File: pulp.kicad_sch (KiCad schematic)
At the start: 0 parts

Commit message: finalized a lot of sub-modules
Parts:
- added C5, C7: 4.7uF, Capacitor_SMD:C_0201_0603Metric, symbol Device:C
- added C6, C8: 1uF, Capacitor_SMD:C_0201_0603Metric, symbol Device:C
- added D1, D2: ESD9B5.0ST5G, Diode_SMD:D_SOD-923, symbol Diode:ESD9B5.0ST5G
- added D3: LED_ARGB, symbol Device:LED_ARGB
- added J2, J3: Conn_01x02_Pin, Connector_PinHeader_2.54mm:PinHeader_1x02_P2.54mm_Horizontal, symbol Connector:Conn_01x02_Pin
- added J4, J5: Conn_01x03_Pin, Connector_PinHeader_2.54mm:PinHeader_1x03_P2.54mm_Horizontal, symbol Connector:Conn_01x03_Pin
- added J6: Conn_01x09_Pin, symbol Connector:Conn_01x09_Pin
- added J7: USB_C_Receptacle, Connector_USB:USB_C_Receptacle_CNCTech_C-ARA1-AK51X, symbol Connector:USB_C_Receptacle
- added Q1, Q2, Q3: BSS138, Package_TO_SOT_SMD:SOT-23, symbol Transistor_FET:BSS138
- added R19, R20, R9: 510, symbol Device:R
- added R21, R22, R23: 27, symbol Device:R
- added R4, R5: 5.1K, symbol Device:R
- added R6: 10K, Resistor_SMD:R_0201_0603Metric, symbol Device:R
- added R7, R8: 1K, symbol Device:R
- added SW1, SW2: SW_Push, symbol Switch:SW_Push
- added U4: AP7361C-33E, Package_TO_SOT_SMD:SOT-223-3_TabPin2, symbol Regulator_Linear:AP7361C-33E
- added U5: W25Q128JVS, Package_SO:SOIC-8_5.23x5.23mm_P1.27mm, symbol Memory_Flash:W25Q128JVS
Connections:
- new net: Q2.3 (D), R19.1
- new net: D3.3 (GK), R19.2
- new net: J7.B5 (CC2), R4.1
- new net: Q3.3 (D), R9.1
- new net: D3.4 (BK), R9.2
- new net: Q1.1 (G), R21.2
- new net: Q1.3 (D), R20.1
- new net: D3.2 (RK), R20.2
- new net: Q2.1 (G), R22.2
- new net: J7.A5 (CC1), R5.1
- new net: Q3.1 (G), R23.2
- new net: R7.1, SW2.2
- new net: R8.1, SW1.2
- new net +5V: C5.1, C6.1, D3.1 (A), J6.2 (Pin_2), J7.A4 (VBUS), J7.A9 (VBUS), J7.B4 (VBUS), J7.B9 (VBUS), U4.1 (VI)
- new net 3V3: C7.1, C8.2, J6.3 (Pin_3), R6.2, U4.3 (VO), U5.8 (VCC)
- new net BATT_V: J4.3 (Pin_3), J5.3 (Pin_3)
- new net GND: C5.2, C6.2, C7.2, C8.1, D1.1 (A1), D2.1 (A1), J4.1 (Pin_1), J5.1 (Pin_1), J6.1 (Pin_1), J7.A1 (GND), J7.A12 (GND), J7.B1 (GND), J7.B12 (GND), Q1.2 (S), Q2.2 (S), Q3.2 (S), R4.2, R5.2, SW1.1, SW2.1, U4.2 (GND), U5.4 (GND)
- new net GP0: J6.4 (Pin_4)
- new net GP1: J6.5 (Pin_5)
- new net GP2: J6.6 (Pin_6)
- new net GP3: J6.7 (Pin_7)
- new net GP4: J6.8 (Pin_8)
- new net GP5: J6.9 (Pin_9)
- new net I2C_SCL 0: J3.2 (Pin_2)
- new net I2C_SCL 1: J2.2 (Pin_2)
- new net I2C_SDA 0: J3.1 (Pin_1)
- new net I2C_SDA 1: J2.1 (Pin_1)
- new net LED_B: R23.1
- new net LED_G: R22.1
- new net LED_R: R21.1
- new net PWM_LEFT: J5.2 (Pin_2)
- new net PWM_RIGHT: J4.2 (Pin_2)
- new net Q0: U5.5 (DI(IO0))
- new net Q1: U5.2 (DO(IO1))
- new net Q2: U5.3 (IO2)
- new net Q3: U5.7 (IO3)
- new net Q_SCLK: U5.6 (CLK)
- new net Q_SS: R6.1, R8.2, U5.1 (~{CS})
- new net USB_D+: D1.2 (A2), J7.A6 (D+), J7.B6 (D+)
- new net USB_D-: D2.2 (A2), J7.A7 (D-), J7.B7 (D-)
- new net ~{RST}: R7.2
- no-connect marks 0 -> 11
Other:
- sheet RP2040 ports: added LED_B (GPIO_17), LED_G (GPIO_16), LED_R (GPIO_15); removed SWCLK, SWD
- note added: "I2C 0"
- note added: "I2C 1"

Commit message: NO ERC ERRORS!!!!
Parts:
- D3: footprint (none) -> LED_SMD:LED_RGB_1210
- J6: footprint (none) -> Connector_PinHeader_2.54mm:PinHeader_1x09_P2.54mm_Vertical
- R19, R20, R21, R22, R23, R4, R5, R7, R8, R9: footprint (none) -> Resistor_SMD:R_0201_0603Metric
- SW1, SW2: footprint (none) -> Button_Switch_SMD:SW_Push_SPST_NO_Alps_SKRK
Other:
- sheet MAX_8C GNSS ports: added none; removed SCL, SDA
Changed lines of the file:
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@@
       (effects (font (size 1.27 1.27)))
     )
-    (property "Footprint" "" (at 257.048 39.37 90)
+    (property "Footprint" "Resistor_SMD:R_0201_0603Metric" (at 257.048 39.37 90)
       (effects (font (size 1.27 1.27)) hide)
     )
@@
       (effects (font (size 1.27 1.27)))
     )
-    (property "Footprint" "" (at 64.262 43.18 90)
+    (property "Footprint" "Resistor_SMD:R_0201_0603Metric" (at 64.262 43.18 90)
       (effects (font (size 1.27 1.27)) hide)
     )
@@
       (effects (font (size 1.27 1.27)))
     )
-    (property "Footprint" "" (at 262.128 39.37 90)
+    (property "Footprint" "Resistor_SMD:R_0201_0603Metric" (at 262.128 39.37 90)
       (effects (font (size 1.27 1.27)) hide)
     )
@@
       (effects (font (size 1.27 1.27)))
     )
-    (property "Footprint" "" (at 251.968 39.37 90)
+    (property "Footprint" "Resistor_SMD:R_0201_0603Metric" (at 251.968 39.37 90)
       (effects (font (size 1.27 1.27)) hide)
     )
@@
       (effects (font (size 1.27 1.27)))
     )
-    (property "Footprint" "" (at 69.342 43.18 90)
+    (property "Footprint" "Resistor_SMD:R_0201_0603Metric" (at 69.342 43.18 90)
       (effects (font (size 1.27 1.27)) hide)
     )
@@
       (effects (font (size 1.27 1.27)))
     )
-    (property "Footprint" "" (at 200.66 152.908 90)
+    (property "Footprint" "Resistor_SMD:R_0201_0603Metric" (at 200.66 152.908 90)
       (effects (font (size 1.27 1.27)) hide)
     )
@@
       (effects (font (size 1.27 1.27)))
     )
-    (property "Footprint" "" (at 240.03 53.848 90)
+    (property "Footprint" "Resistor_SMD:R_0201_0603Metric" (at 240.03 53.848 90)
       (effects (font (size 1.27 1.27)) hide)
     )
@@
       (effects (font (size 1.27 1.27)))
     )
-    (property "Footprint" "" (at 256.54 26.67 0)
+    (property "Footprint" "LED_SMD:LED_RGB_1210" (at 256.54 26.67 0)
       (effects (font (size 1.27 1.27)) hide)
     )
@@
       (effects (font (size 1.27 1.27)))
     )
-    (property "Footprint" "" (at 200.66 140.208 90)
+    (property "Footprint" "Resistor_SMD:R_0201_0603Metric" (at 200.66 140.208 90)
       (effects (font (size 1.27 1.27)) hide)
     )
@@
       (effects (font (size 1.27 1.27)))
     )
-    (property "Footprint" "" (at 187.96 133.35 0)
+    (property "Footprint" "Button_Switch_SMD:SW_Push_SPST_NO_Alps_SKRK" (at 187.96 133.35 0)
       (effects (font (size 1.27 1.27)) hide)
     )
@@
       (effects (font (size 1.27 1.27)))
     )
-    (property "Footprint" "" (at 240.03 64.008 90)
+    (property "Footprint" "Resistor_SMD:R_0201_0603Metric" (at 240.03 64.008 90)
       (effects (font (size 1.27 1.27)) hide)
     )
@@
       (effects (font (size 1.27 1.27)))
     )
-    (property "Footprint" "" (at 240.03 74.168 90)
+    (property "Footprint" "Resistor_SMD:R_0201_0603Metric" (at 240.03 74.168 90)
       (effects (font (size 1.27 1.27)) hide)
     )
@@
       (effects (font (size 1.27 1.27)))
     )
-    (property "Footprint" "" (at 187.96 146.05 0)
+    (property "Footprint" "Button_Switch_SMD:SW_Push_SPST_NO_Alps_SKRK" (at 187.96 146.05 0)
       (effects (font (size 1.27 1.27)) hide)
     )
@@
       (effects (font (size 1.27 1.27)) (justify right))
     )
-    (property "Footprint" "" (at 232.41 147.32 0)
+    (property "Footprint" "Connector_PinHeader_2.54mm:PinHeader_1x09_P2.54mm_Vertical" (at 232.41 147.32 0)
       (effects (font (size 1.27 1.27)) hide)
     )
@@
       (effects (font (size 1.27 1.27)) (justify left))
     )
-    (pin "SDA" input (at 177.8 90.17 180)
-      (effects (font (size 1.27 1.27)) (justify left))
-    )
-    (pin "SCL" input (at 177.8 87.63 180)
-      (effects (font (size 1.27 1.27)) (justify left))
-    )

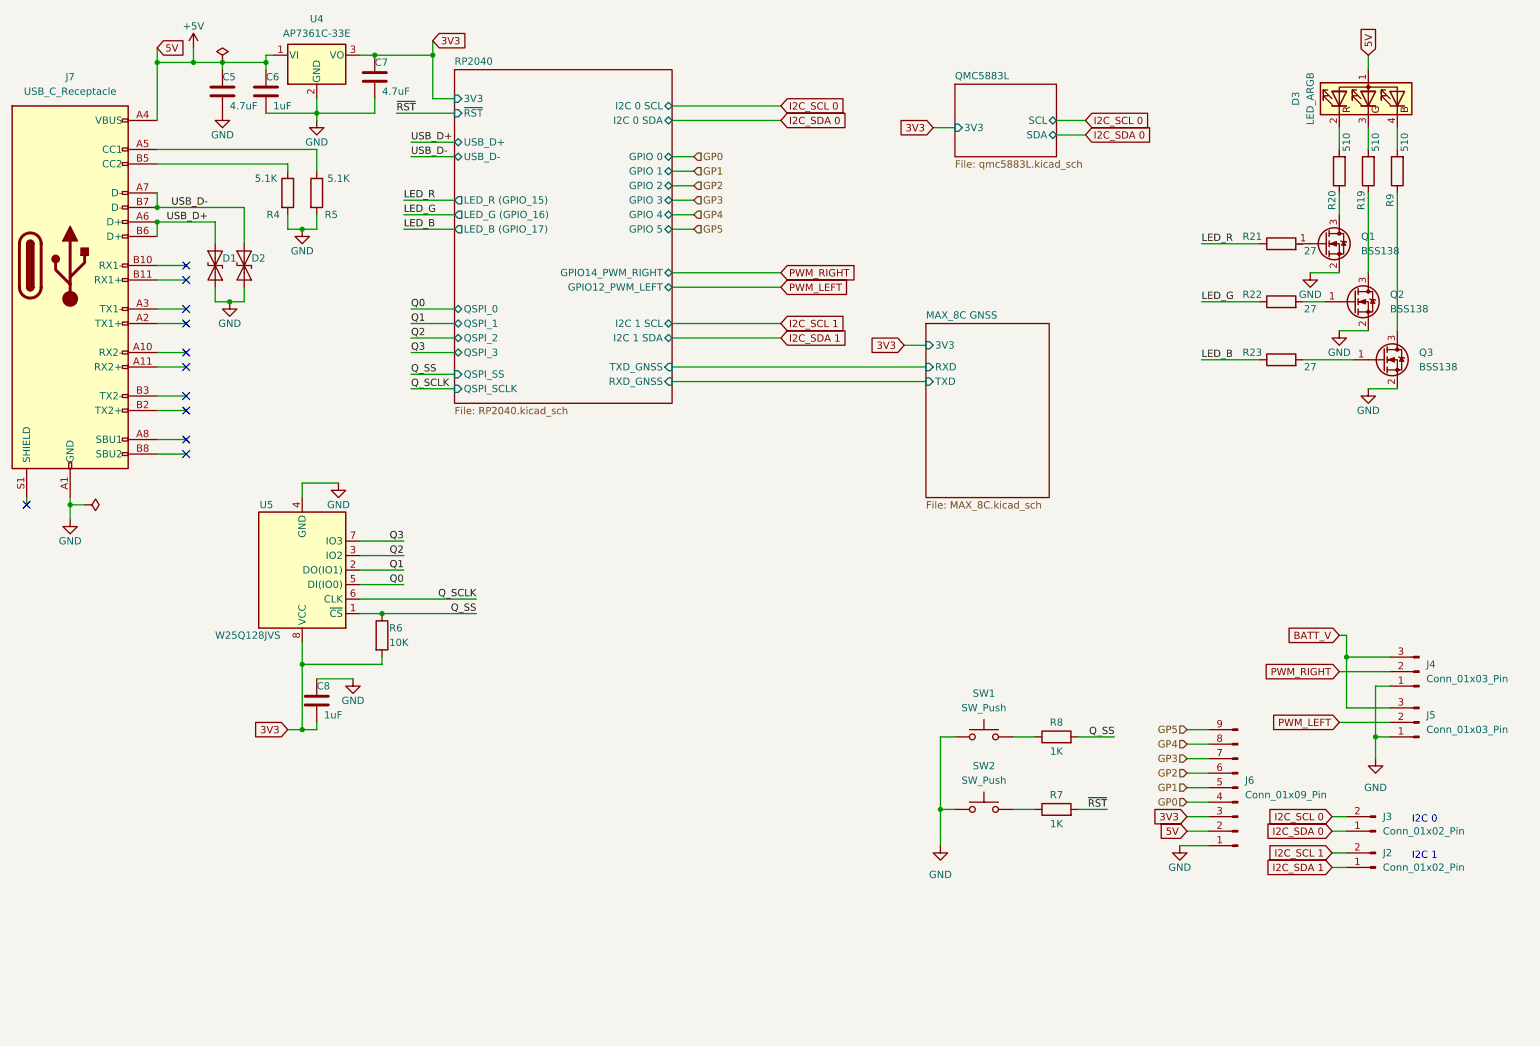
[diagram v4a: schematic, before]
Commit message: Finalized voltage regulator for Battery
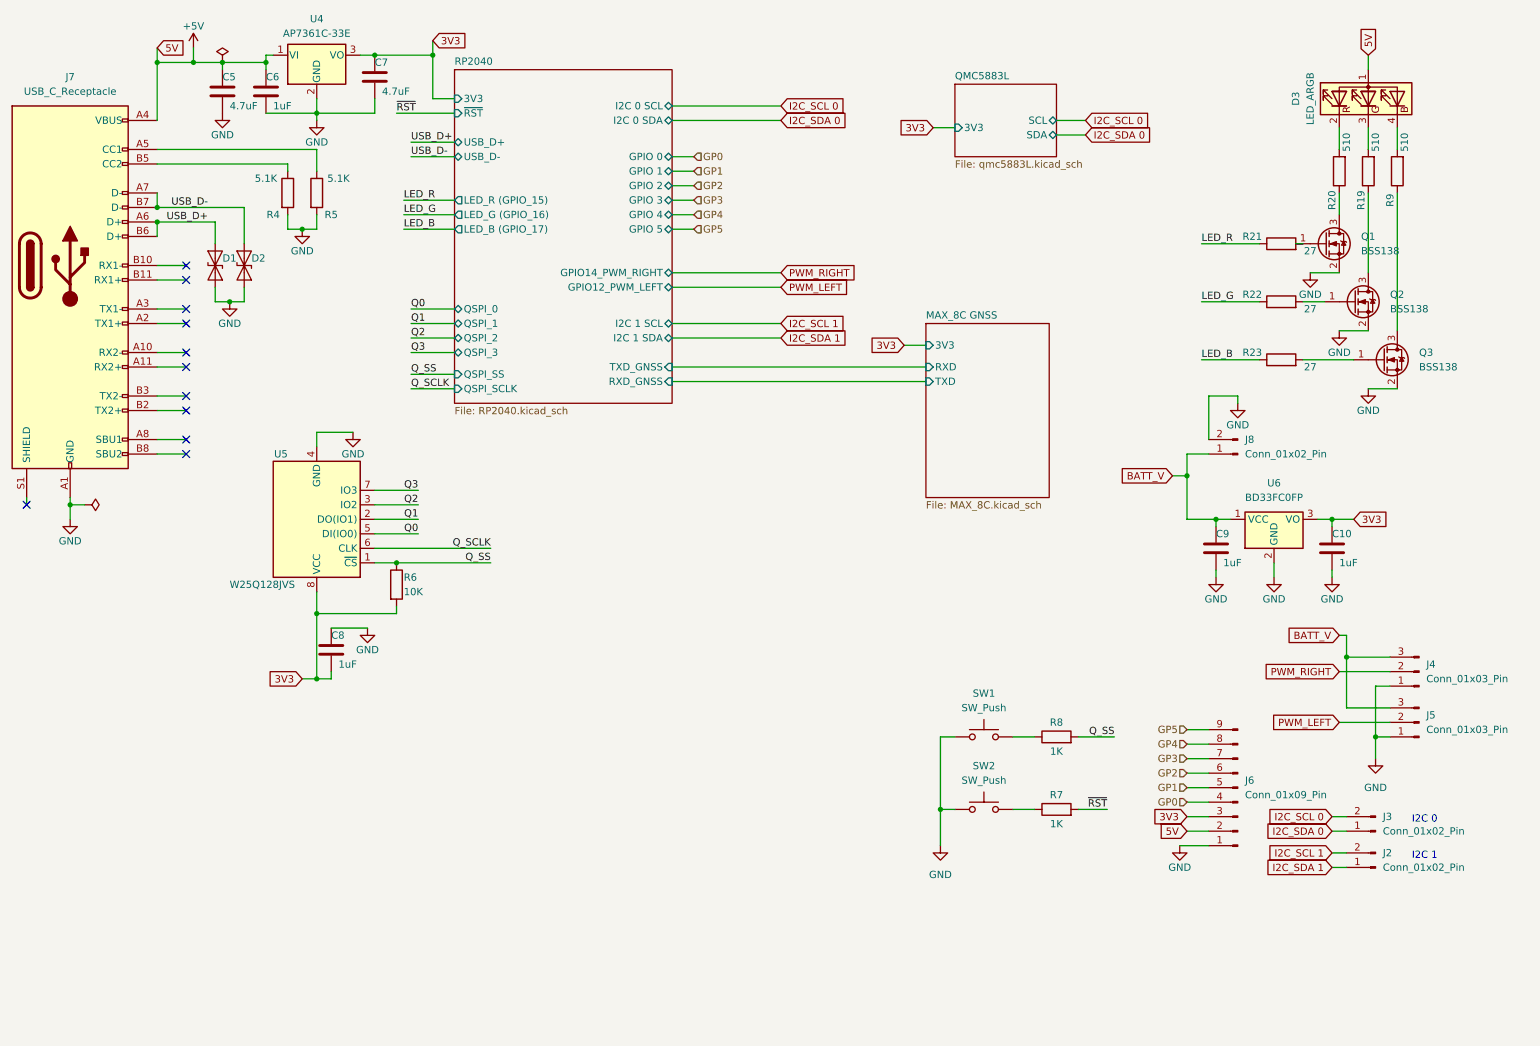
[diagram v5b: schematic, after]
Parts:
- added C10, C9: 1uF, Capacitor_SMD:C_0201_0603Metric, symbol Device:C
- added J8: Conn_01x02_Pin, Connector_AMASS:AMASS_XT60-F_1x02_P7.20mm_Vertical, symbol Connector:Conn_01x02_Pin
- added U6: BD33FC0FP, Package_TO_SOT_SMD:TO-252-2, symbol Regulator_Linear:BD33FC0FP
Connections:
- net 3V3: now also C10.1, U6.3 (VO)
- net BATT_V: now also C9.1, J8.1 (Pin_1), U6.1 (VCC)
- net GND: now also C10.2, C9.2, J8.2 (Pin_2), U6.2 (GND)
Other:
- moved on the sheet: C8, R6, U5

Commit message: begins PCB routing for the final design V1
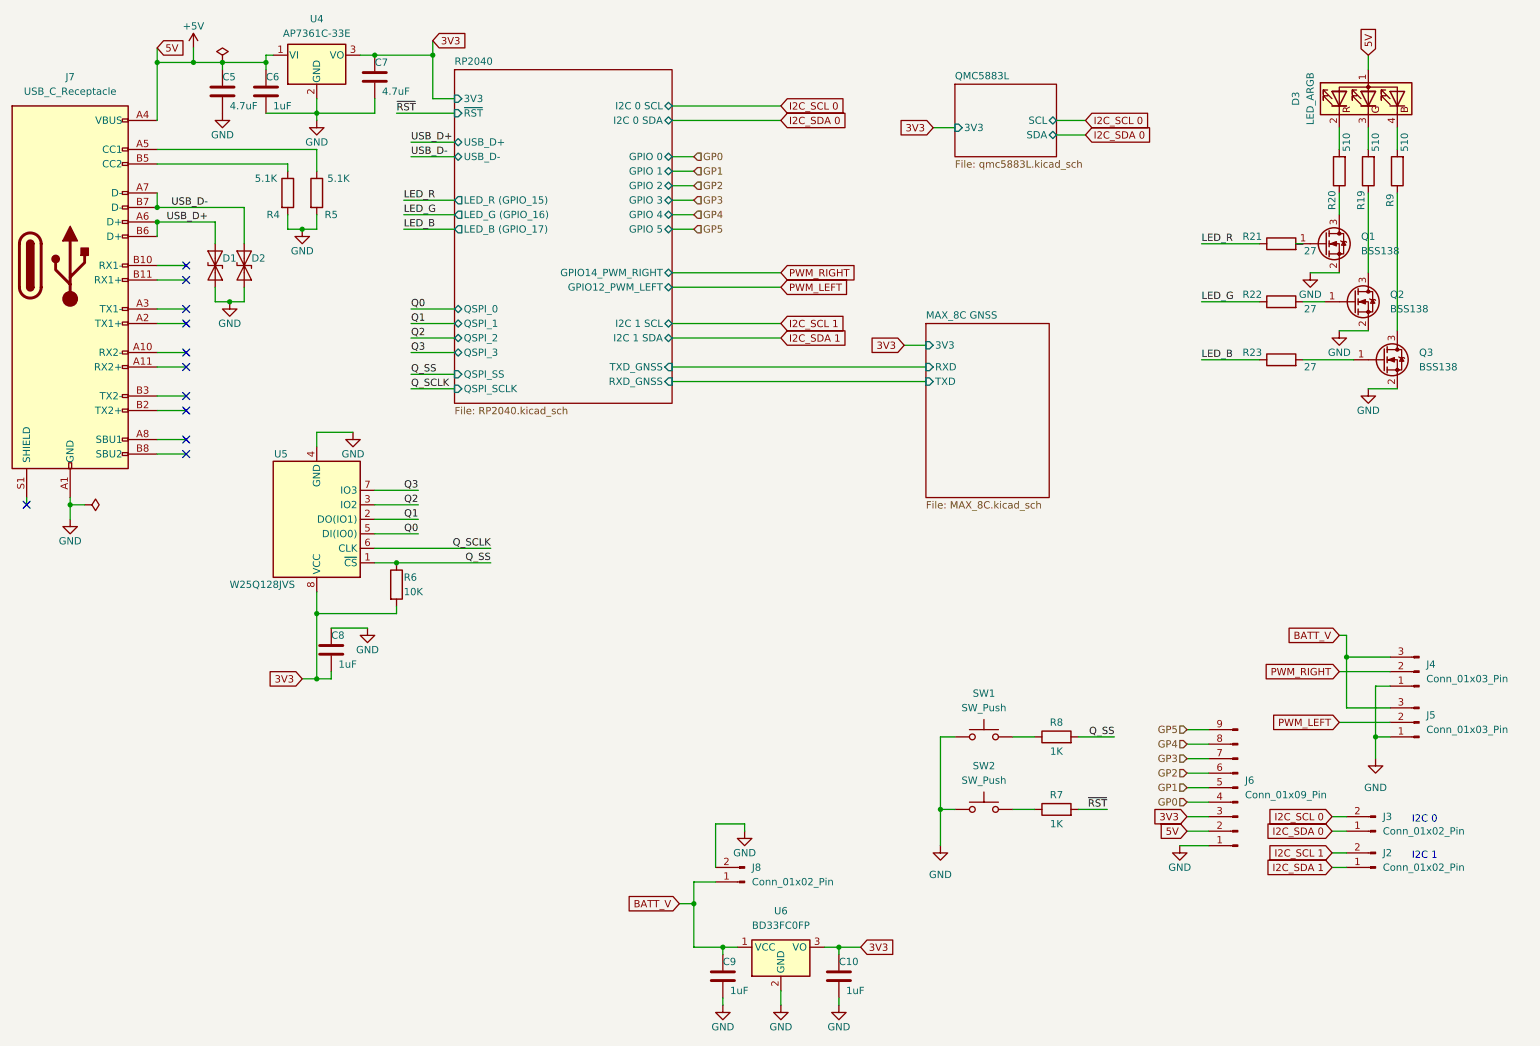
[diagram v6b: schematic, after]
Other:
- moved on the sheet: C10, C9, J8, U6

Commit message: finished pcb layout
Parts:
- removed C10, C9: 1uF, Capacitor_SMD:C_0201_0603Metric, symbol Device:C
- removed J8: Conn_01x02_Pin, Connector_AMASS:AMASS_XT60-F_1x02_P7.20mm_Vertical, symbol Connector:Conn_01x02_Pin
- removed U6: BD33FC0FP, Package_TO_SOT_SMD:TO-252-2, symbol Regulator_Linear:BD33FC0FP
- added D4: 1A, Diode_SMD:D_1812_4532Metric, symbol Device:D
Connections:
- net BATT_V is gone; now on net +5V: J4.3 (Pin_3), J5.3 (Pin_3)
- net +5V: now also D4.1 (K); no longer J7.A4 (VBUS), J7.A9 (VBUS), J7.B4 (VBUS), J7.B9 (VBUS)
- net I2C_SCL 0: now also J3.1 (Pin_1); no longer J3.2 (Pin_2)
- net I2C_SCL 1: now also J2.1 (Pin_1); no longer J2.2 (Pin_2)
- net I2C_SDA 0: now also J3.2 (Pin_2); no longer J3.1 (Pin_1)
- net I2C_SDA 1: now also J2.2 (Pin_2); no longer J2.1 (Pin_1)
- new net: D4.2 (A), J7.A4 (VBUS), J7.A9 (VBUS), J7.B4 (VBUS), J7.B9 (VBUS)
